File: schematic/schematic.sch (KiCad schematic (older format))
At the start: 4 parts

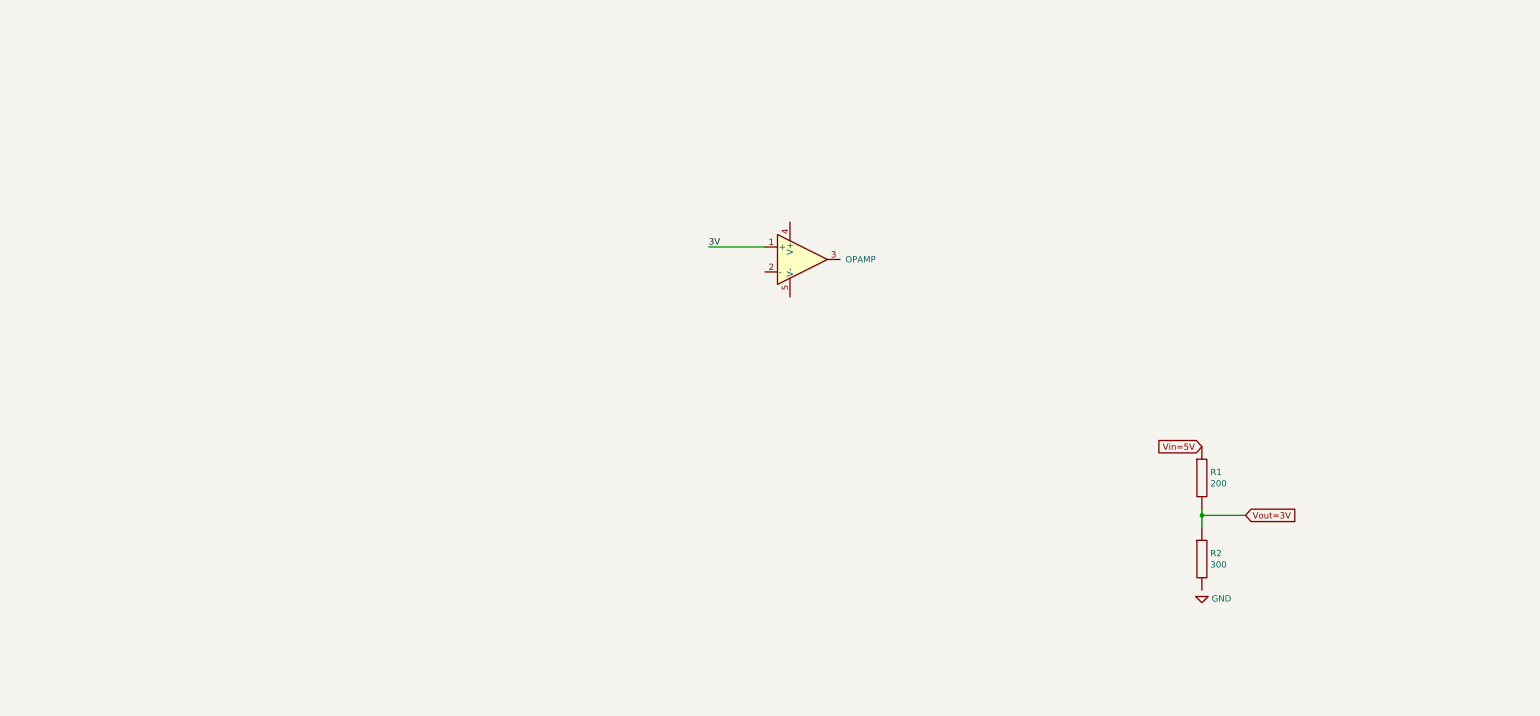
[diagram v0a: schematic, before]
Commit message: some schem work
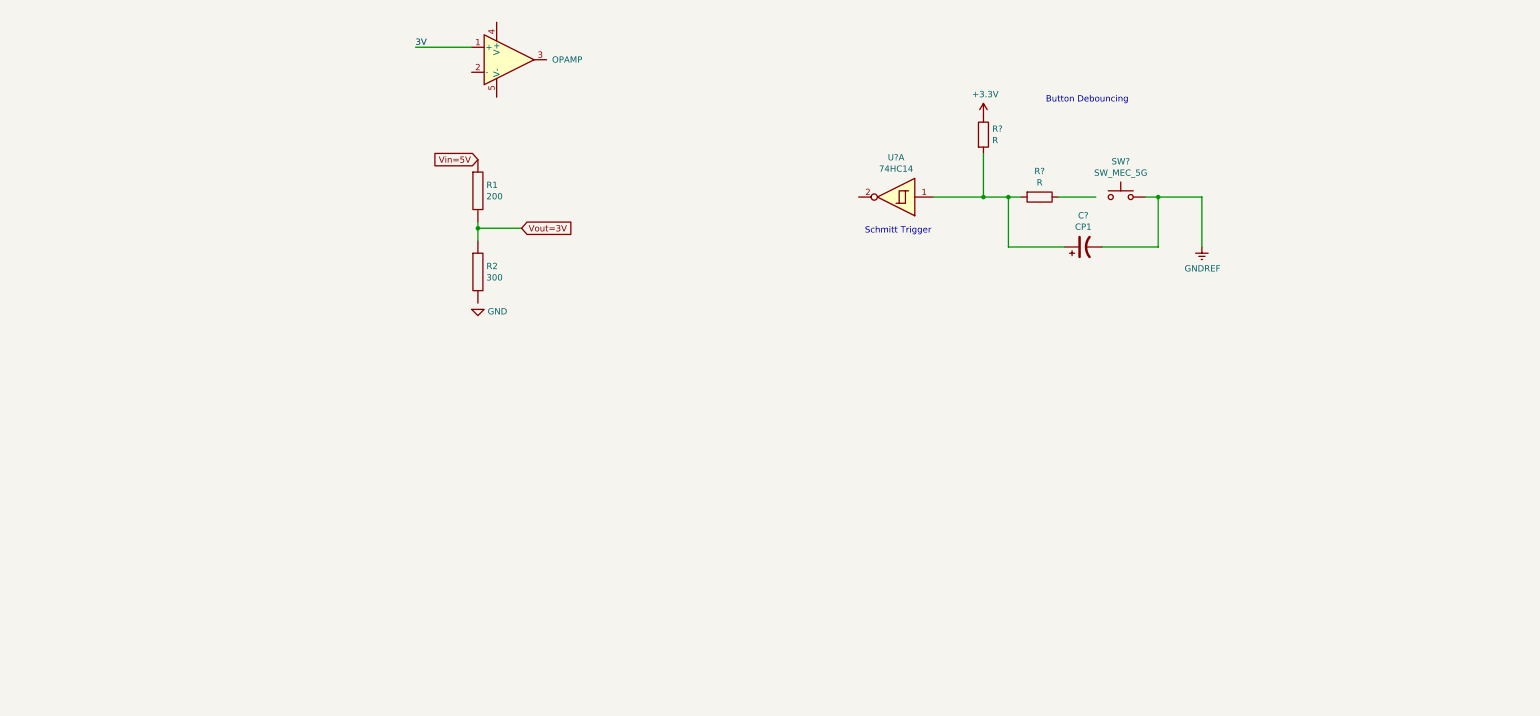
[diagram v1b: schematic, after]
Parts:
- added C?: CP1, symbol Device:CP1
- added R? (x2): R, symbol Device:R
- added SW?: SW_MEC_5G, symbol Switch:SW_MEC_5G
- added U?: 74HC14, symbol 74xx:74HC14
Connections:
- new net: C?.1, R?.2, R?.2, U?.1
- new net: R?.1, SW?.1 (A), SW?.2 (A)
- new net +3V3: R?.1
- new net GNDREF: C?.2, SW?.3 (B), SW?.4 (B)
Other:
- note added: "Button Debouncing\n"
- note added: "Schmitt Trigger\n"
- moved on the sheet: R1, R2
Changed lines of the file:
@@
 L pspice:OPAMP OpAmp1
 U 1 1 61FD4970
-P 4300 3100
-F 0 "OpAmp1" H 4644 3146 50  0001 L CNN
-F 1 "OPAMP" H 4644 3100 50  0000 L CNN
-F 2 "" H 4300 3100 50  0001 C CNN
-F 3 "~" H 4300 3100 50  0001 C CNN
-	1    4300 3100
+P 1950 1500
+F 0 "OpAmp1" H 2294 1546 50  0001 L CNN
+F 1 "OPAMP" H 2294 1500 50  0000 L CNN
+F 2 "" H 1950 1500 50  0001 C CNN
+F 3 "~" H 1950 1500 50  0001 C CNN
+	1    1950 1500
 	1    0    0    -1
 $EndComp
 Wire Wire Line
-	4000 3000 3550 3000
-Text Label 3550 3000 0    50   ~ 0
+	1650 1400 1200 1400
+Text Label 1200 1400 0    50   ~ 0
 3V
 $Comp
 L pspice:R R1
 U 1 1 61FD5327
-P 7500 4850
-F 0 "R1" H 7568 4896 50  0000 L CNN
-F 1 "200" H 7568 4805 50  0000 L CNN
-F 2 "" H 7500 4850 50  0001 C CNN
-F 3 "~" H 7500 4850 50  0001 C CNN
-	1    7500 4850
+P 1700 2550
+F 0 "R1" H 1768 2596 50  0000 L CNN
+F 1 "200" H 1768 2505 50  0000 L CNN
+F 2 "" H 1700 2550 50  0001 C CNN
+F 3 "~" H 1700 2550 50  0001 C CNN
+	1    1700 2550
 	1    0    0    -1
 $EndComp
-Text GLabel 7500 4600 0    50   Input ~ 0
+Text GLabel 1700 2300 0    50   Input ~ 0
 Vin=5V
 Wire Wire Line
-	7500 5100 7500 5150
-Connection ~ 7500 5150
+	1700 2800 1700 2850
+Connection ~ 1700 2850
 Wire Wire Line
-	7500 5150 7500 5250
+	1700 2850 1700 2950
 Wire Wire Line
-	7500 5150 7850 5150
-Text GLabel 7850 5150 2    50   Input ~ 0
+	1700 2850 2050 2850
+Text GLabel 2050 2850 2    50   Input ~ 0
 Vout=3V
 $Comp
 L pspice:R R2
 U 1 1 61FD5B76
-P 7500 5500
-F 0 "R2" H 7568 5546 50  0000 L CNN
-F 1 "300" H 7568 5455 50  0000 L CNN
-F 2 "" H 7500 5500 50  0001 C CNN
-F 3 "~" H 7500 5500 50  0001 C CNN
-	1    7500 5500
+P 1700 3200
+F 0 "R2" H 1768 3246 50  0000 L CNN
+F 1 "300" H 1768 3155 50  0000 L CNN
+F 2 "" H 1700 3200 50  0001 C CNN
+F 3 "~" H 1700 3200 50  0001 C CNN
+	1    1700 3200
 	1    0    0    -1
 $EndComp
@@
 L pspice:0 GND
 U 1 1 61FD6CC4
-P 7500 5800
-F 0 "GND" H 7578 5783 50  0000 L CNN
-F 1 "0" H 7500 5889 50  0001 C CNN
-F 2 "" H 7500 5800 50  0001 C CNN
-F 3 "~" H 7500 5800 50  0001 C CNN
-	1    7500 5800
+P 1700 3500
+F 0 "GND" H 1778 3483 50  0000 L CNN
+F 1 "0" H 1700 3589 50  0001 C CNN
+F 2 "" H 1700 3500 50  0001 C CNN
+F 3 "~" H 1700 3500 50  0001 C CNN
+	1    1700 3500
 	1    0    0    -1
 $EndComp
+Text Notes 6250 1850 0    50   ~ 0
+Button Debouncing\n
+$Comp
+L power:+3.3V #PWR?
+U 1 1 6207136F
+P 5750 1950
+F 0 "#PWR?" H 5750 1800 50  0001 C CNN
+F 1 "+3.3V" H 5765 2123 50  0000 C CNN
+F 2 "" H 5750 1950 50  0001 C CNN
+F 3 "" H 5750 1950 50  0001 C CNN
+	1    5750 1950
+	1    0    0    -1
+$EndComp
+$Comp
+L 74xx:74HC14 U?
+U 1 1 6207415B
+P 5050 2600
+F 0 "U?" H 5050 2283 50  0000 C CNN
+F 1 "74HC14" H 5050 2374 50  0000 C CNN
+F 2 "" H 5050 2600 50  0001 C CNN
+F 3 "http://www.ti.com/lit/gpn/sn74HC14" H 5050 2600 50  0001 C CNN
+	1    5050 2600
+	-1   0    0    1
+$EndComp
+Text Notes 4800 2900 0    50   ~ 0
+Schmitt Trigger\n
+$Comp
+L Device:R R?
+U 1 1 62076385
+P 5750 2100
+F 0 "R?" H 5820 2146 50  0000 L CNN
+F 1 "R" H 5820 2055 50  0000 L CNN
+F 2 "" V 5680 2100 50  0001 C CNN
+F 3 "~" H 5750 2100 50  0001 C CNN
+	1    5750 2100
+	1    0    0    -1
+$EndComp
+$Comp
+L Device:R R?
+U 1 1 6207695D
+P 6200 2600
+F 0 "R?" V 5993 2600 50  0000 C CNN
+F 1 "R" V 6084 2600 50  0000 C CNN
+F 2 "" V 6130 2600 50  0001 C CNN
+F 3 "~" H 6200 2600 50  0001 C CNN
+	1    6200 2600
+	0    1    1    0
+$EndComp
+$Comp
+L Switch:SW_MEC_5G SW?
+U 1 1 62077CD9
+P 6850 2600
+F 0 "SW?" H 6850 2885 50  0000 C CNN
+F 1 "SW_MEC_5G" H 6850 2794 50  0000 C CNN
+F 2 "" H 6850 2800 50  0001 C CNN
+F 3 "http://www.apem.com/int/index.php?controller=attachment&id_attachment=488" H 6850 2800 50  0001 C CNN
+	1    6850 2600
+	1    0    0    -1
+$EndComp
+$Comp
+L Device:CP1 C?
+U 1 1 6207934D
+P 6550 3000
+F 0 "C?" V 6802 3000 50  0000 C CNN
+F 1 "CP1" V 6711 3000 50  0000 C CNN
+F 2 "" H 6550 3000 50  0001 C CNN
+F 3 "~" H 6550 3000 50  0001 C CNN
+	1    6550 3000
+	0    -1   -1   0
+$EndComp
+$Comp
+L power:GNDREF #PWR?
+U 1 1 6207A1A4
+P 7500 3000
+F 0 "#PWR?" H 7500 2750 50  0001 C CNN
+F 1 "GNDREF" H 7505 2827 50  0000 C CNN
+F 2 "" H 7500 3000 50  0001 C CNN
+F 3 "" H 7500 3000 50  0001 C CNN
+	1    7500 3000
+	1    0    0    -1
+$EndComp
+Wire Wire Line
+	5750 2250 5750 2600
+Wire Wire Line
+	5750 2600 5350 2600
+Wire Wire Line
+	5750 2600 5950 2600
+Connection ~ 5750 2600
+Wire Wire Line
+	6350 2600 6650 2600
+Wire Wire Line
+	7050 2600 7150 2600
+Wire Wire Line
+	7500 2600 7500 3000
+Wire Wire Line
+	6700 3000 7150 3000
+Wire Wire Line
+	6400 3000 5950 3000
+Wire Wire Line
+	5950 3000 5950 2600
+Connection ~ 5950 2600
+Wire Wire Line
+	5950 2600 6050 2600
+Wire Wire Line
+	7150 3000 7150 2600
+Connection ~ 7150 2600
+Wire Wire Line
+	7150 2600 7500 2600
 $EndSCHEMATC

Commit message: PCB started
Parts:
- removed C?: CP1, symbol Device:CP1
- removed R? (x2): R, symbol Device:R
- removed SW?: SW_MEC_5G, symbol Switch:SW_MEC_5G
- removed U?: 74HC14, symbol 74xx:74HC14
- added ANT? (x2): ESP32-WROOM-32D, ESP32WROOM32D, symbol Noggin:ESP32-WROOM-32D
- added C? (x2): CP1, symbol Device:CP1
- added D? (x3): LED, symbol Device:LED
- added LS?: PS1240P02BT, PS1240P02BT, symbol Noggin:PS1240P02BT
- added R? (x4): R, symbol Device:R
- added R?: 1K, symbol Device:R
- added SW? (x2): SW_MEC_5G, symbol Switch:SW_MEC_5G
- added U?: SEN-11574, symbol Noggin:SEN-11574
- added U? (x2): 74HC14, symbol 74xx:74HC14
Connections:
- net +3V3: now also ANT?.2 (3V3), ANT?.2 (3V3), R?.1, R?.1, U?.~ (VDD)
- net GNDREF: now also C?.2, C?.2, SW?.3 (B), SW?.3 (B), SW?.4 (B), SW?.4 (B)
- new net: ANT?.10 (IO25), D?.2 (A)
- new net: ANT?.11 (IO26), D?.2 (A)
- new net: ANT?.12 (IO27), U?.2
- new net: ANT?.23 (IO15), U?.~ (VDD)
- new net: ANT?.27 (IO16), R?.2
- new net: C?.1, R?.2, R?.2, U?.1 (x2)
- new net: R?.1, SW?.1 (A), SW?.2 (A) (x2)
- new net: LS?.1, R?.1
- new net: ANT?.6 (IO34), D?.2 (A)
- new net: ANT?.9 (IO33), U?.2
- new net GND: ANT?.1 (GND_1), D?.1 (K), D?.1 (K), D?.1 (K), LS?.2, U?.~ (VDD)
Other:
- note added: "Supervisor\n"
- note added: "Wearer\n"
- moved on the sheet: R1, R2
